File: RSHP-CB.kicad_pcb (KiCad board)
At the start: 2 copper layers, 140 x 120 mm, 23 parts, among them J1 Conn_02x20_Odd_Even, J2 Conn_02x02_Odd_Even, J3 Conn_02x02_Odd_Even, J4 Conn_02x04_Odd_Even

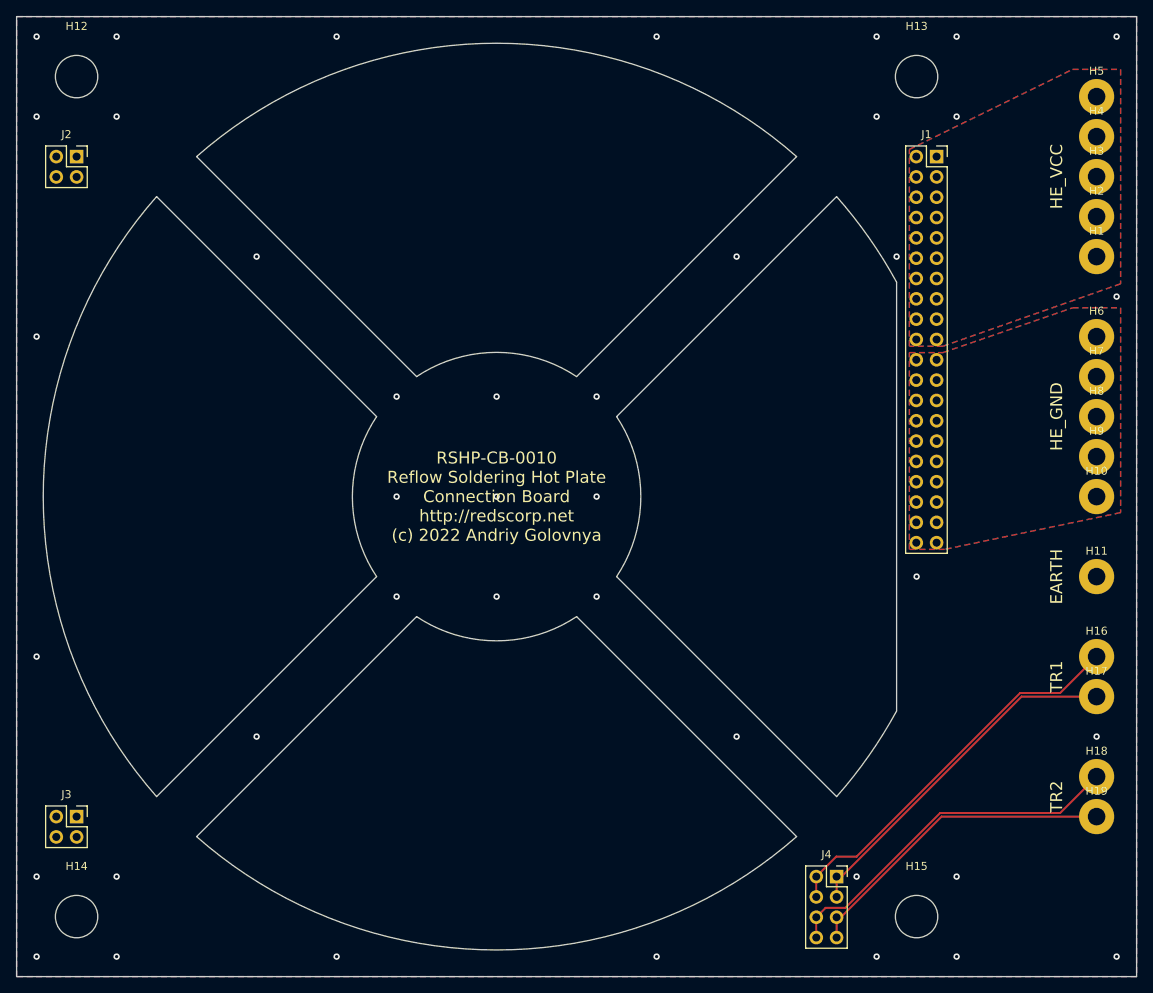
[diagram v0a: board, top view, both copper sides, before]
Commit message: Moved some stuff around on schematics. Added descriptive texts on schematics. Made mount holed current transmissible. Hidden solder and mount holes's designators.
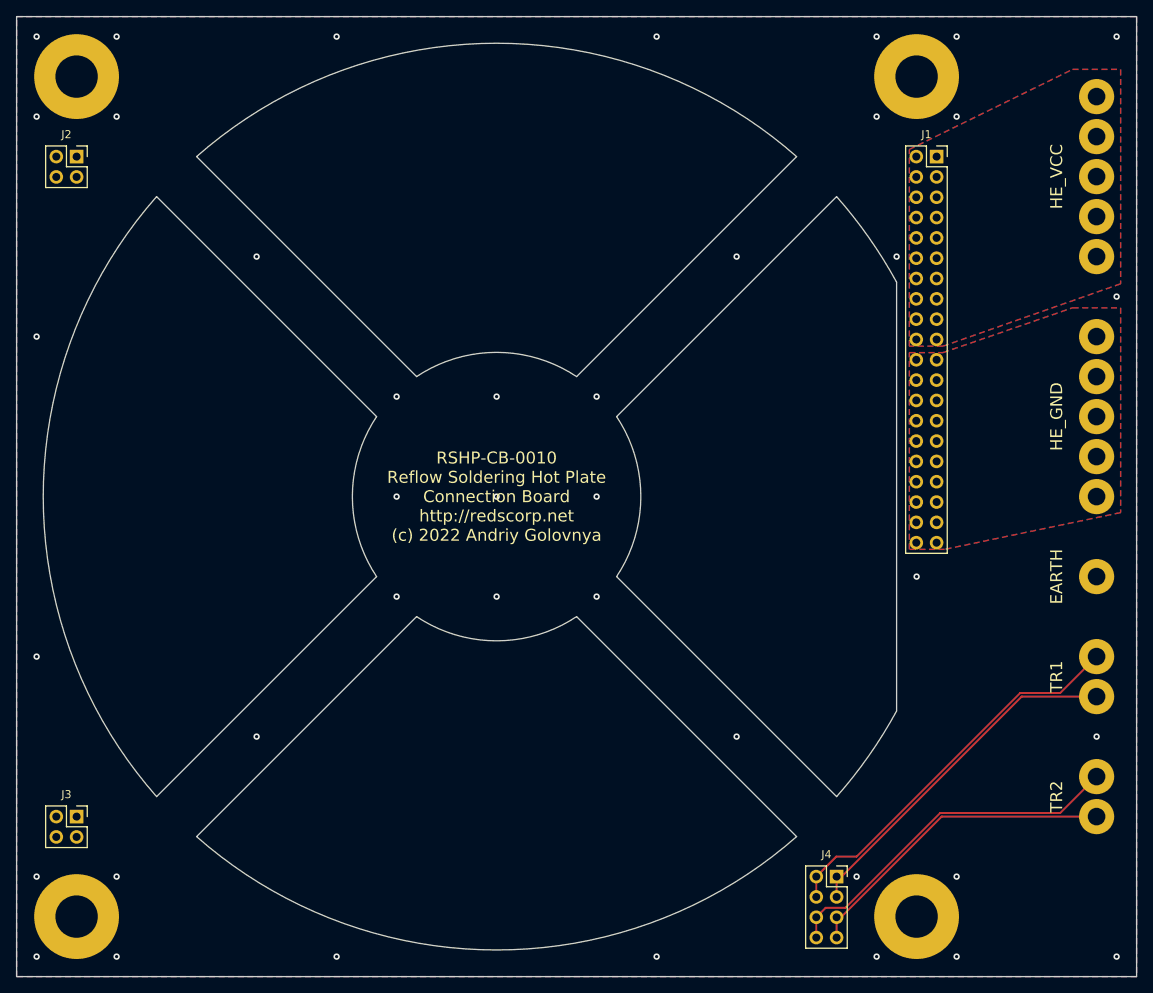
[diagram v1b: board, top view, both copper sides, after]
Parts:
- H12, H13, H14, H15: footprint MountingHole:MountingHole_5.3mm_M5 -> MountingHole:MountingHole_5.3mm_M5_Pad
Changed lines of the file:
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@@
     (property "Sheetname" "")
     (attr exclude_from_pos_files)
-    (fp_text reference "H3" (at 0 -3.2) (layer "F.SilkS")
+    (fp_text reference "H3" (at 0 -3.2) (layer "F.SilkS") hide
       (effects (font (size 1 1) (thickness 0.15)))
     )
@@
     (property "Sheetname" "")
     (attr exclude_from_pos_files)
-    (fp_text reference "H19" (at 0 -3.2) (layer "F.SilkS")
+    (fp_text reference "H19" (at 0 -3.2) (layer "F.SilkS") hide
       (effects (font (size 1 1) (thickness 0.15)))
     )
@@
     (property "Sheetname" "")
     (attr exclude_from_pos_files)
-    (fp_text reference "H18" (at 0 -3.2) (layer "F.SilkS")
+    (fp_text reference "H18" (at 0 -3.2) (layer "F.SilkS") hide
       (effects (font (size 1 1) (thickness 0.15)))
     )
@@
     (property "Sheetname" "")
     (attr exclude_from_pos_files)
-    (fp_text reference "H10" (at 0 -3.2) (layer "F.SilkS")
+    (fp_text reference "H10" (at 0 -3.2) (layer "F.SilkS") hide
       (effects (font (size 1 1) (thickness 0.15)))
     )
@@
     (property "Sheetname" "")
     (attr exclude_from_pos_files)
-    (fp_text reference "H16" (at 0 -3.2) (layer "F.SilkS")
+    (fp_text reference "H16" (at 0 -3.2) (layer "F.SilkS") hide
       (effects (font (size 1 1) (thickness 0.15)))
     )
@@
     (property "Sheetname" "")
     (attr exclude_from_pos_files)
-    (fp_text reference "H8" (at 0 -3.2) (layer "F.SilkS")
+    (fp_text reference "H8" (at 0 -3.2) (layer "F.SilkS") hide
       (effects (font (size 1 1) (thickness 0.15)))
     )
@@
       (net 2 "HE_GND") (pinfunction "1") (pintype "input"))
   )
-  (footprint "MountingHole:MountingHole_5.3mm_M5" (layer "F.Cu")
+  (footprint "MountingHole:MountingHole_5.3mm_M5_Pad" (layer "F.Cu")
     (at 57.5 142.5)
-    (descr "Mounting Hole 5.3mm, no annular, M5")
-    (tags "mounting hole 5.3mm no annular m5")
-    (property "Sheetfile" "RSHP-CB.kicad_sch")
-    (property "Sheetname" "")
-    (attr exclude_from_pos_files)
-    (fp_text reference "H14" (at 0 -6.3) (layer "F.SilkS")
+    (descr "Mounting Hole 5.3mm, M5")
+    (tags "mounting hole 5.3mm m5")
+    (property "Sheetfile" "RSHP-CB.kicad_sch")
+    (property "Sheetname" "")
+    (attr exclude_from_pos_files)
+    (fp_text reference "H14" (at 0 -6.3) (layer "F.SilkS") hide
       (effects (font (size 1 1) (thickness 0.15)))
     )
@@
     (fp_circle (center 0 0) (end 5.3 0) (layer "Cmts.User") (width 0.15) (fill none))
     (fp_circle (center 0 0) (end 5.55 0) (layer "F.CrtYd") (width 0.05) (fill none))
-    (pad "" np_thru_hole circle (at 0 0) (size 5.3 5.3) (drill 5.3) (layers *.Cu *.Mask))
+    (pad "1" thru_hole circle (at 0 0) (size 10.6 10.6) (drill 5.3) (layers *.Cu *.Mask)
+      (net 3 "EARTH") (pinfunction "1") (pintype "input"))
   )
   (footprint "Connector_PinSocket_2.54mm:PinSocket_2x02_P2.54mm_Vertical" (layer "F.Cu")
@@
     (property "Sheetname" "")
     (attr exclude_from_pos_files)
-    (fp_text reference "H6" (at 0 -3.2) (layer "F.SilkS")
+    (fp_text reference "H6" (at 0 -3.2) (layer "F.SilkS") hide
       (effects (font (size 1 1) (thickness 0.15)))
     )
@@
     (property "Sheetname" "")
     (attr exclude_from_pos_files)
-    (fp_text reference "H9" (at 0 -3.2) (layer "F.SilkS")
+    (fp_text reference "H9" (at 0 -3.2) (layer "F.SilkS") hide
       (effects (font (size 1 1) (thickness 0.15)))
     )
@@
       (net 2 "HE_GND") (pinfunction "1") (pintype "input"))
   )
-  (footprint "MountingHole:MountingHole_5.3mm_M5" (layer "F.Cu")
+  (footprint "MountingHole:MountingHole_5.3mm_M5_Pad" (layer "F.Cu")
     (at 57.5 37.5)
-    (descr "Mounting Hole 5.3mm, no annular, M5")
-    (tags "mounting hole 5.3mm no annular m5")
-    (property "Sheetfile" "RSHP-CB.kicad_sch")
-    (property "Sheetname" "")
-    (attr exclude_from_pos_files)
-    (fp_text reference "H12" (at 0 -6.3) (layer "F.SilkS")
+    (descr "Mounting Hole 5.3mm, M5")
+    (tags "mounting hole 5.3mm m5")
+    (property "Sheetfile" "RSHP-CB.kicad_sch")
+    (property "Sheetname" "")
+    (attr exclude_from_pos_files)
+    (fp_text reference "H12" (at 0 -6.3) (layer "F.SilkS") hide
       (effects (font (size 1 1) (thickness 0.15)))
     )
@@
     (fp_circle (center 0 0) (end 5.3 0) (layer "Cmts.User") (width 0.15) (fill none))
     (fp_circle (center 0 0) (end 5.55 0) (layer "F.CrtYd") (width 0.05) (fill none))
-    (pad "" np_thru_hole circle (at 0 0) (size 5.3 5.3) (drill 5.3) (layers *.Cu *.Mask))
-  )
-  (footprint "MountingHole:MountingHole_5.3mm_M5" (layer "F.Cu")
+    (pad "1" thru_hole circle (at 0 0) (size 10.6 10.6) (drill 5.3) (layers *.Cu *.Mask)
+      (net 3 "EARTH") (pinfunction "1") (pintype "input"))
+  )
+  (footprint "MountingHole:MountingHole_5.3mm_M5_Pad" (layer "F.Cu")
     (at 162.5 142.5)
-    (descr "Mounting Hole 5.3mm, no annular, M5")
-    (tags "mounting hole 5.3mm no annular m5")
-    (property "Sheetfile" "RSHP-CB.kicad_sch")
-    (property "Sheetname" "")
-    (attr exclude_from_pos_files)
-    (fp_text reference "H15" (at 0 -6.3) (layer "F.SilkS")
+    (descr "Mounting Hole 5.3mm, M5")
+    (tags "mounting hole 5.3mm m5")
+    (property "Sheetfile" "RSHP-CB.kicad_sch")
+    (property "Sheetname" "")
+    (attr exclude_from_pos_files)
+    (fp_text reference "H15" (at 0 -6.3) (layer "F.SilkS") hide
       (effects (font (size 1 1) (thickness 0.15)))
     )
@@
     (fp_circle (center 0 0) (end 5.3 0) (layer "Cmts.User") (width 0.15) (fill none))
     (fp_circle (center 0 0) (end 5.55 0) (layer "F.CrtYd") (width 0.05) (fill none))
-    (pad "" np_thru_hole circle (at 0 0) (size 5.3 5.3) (drill 5.3) (layers *.Cu *.Mask))
+    (pad "1" thru_hole circle (at 0 0) (size 10.6 10.6) (drill 5.3) (layers *.Cu *.Mask)
+      (net 3 "EARTH") (pinfunction "1") (pintype "input"))
   )
   (footprint "MountingHole:MountingHole_2.2mm_M2_Pad" (layer "F.Cu")
@@
     (property "Sheetname" "")
     (attr exclude_from_pos_files)
-    (fp_text reference "H7" (at 0 -3.2) (layer "F.SilkS")
+    (fp_text reference "H7" (at 0 -3.2) (layer "F.SilkS") hide
       (effects (font (size 1 1) (thickness 0.15)))
     )
@@
       (net 2 "HE_GND") (pinfunction "1") (pintype "input"))
   )
-  (footprint "MountingHole:MountingHole_5.3mm_M5" (layer "F.Cu")
+  (footprint "MountingHole:MountingHole_5.3mm_M5_Pad" (layer "F.Cu")
     (at 162.5 37.5)
-    (descr "Mounting Hole 5.3mm, no annular, M5")
-    (tags "mounting hole 5.3mm no annular m5")
-    (property "Sheetfile" "RSHP-CB.kicad_sch")
-    (property "Sheetname" "")
-    (attr exclude_from_pos_files)
-    (fp_text reference "H13" (at 0 -6.3) (layer "F.SilkS")
+    (descr "Mounting Hole 5.3mm, M5")
+    (tags "mounting hole 5.3mm m5")
+    (property "Sheetfile" "RSHP-CB.kicad_sch")
+    (property "Sheetname" "")
+    (attr exclude_from_pos_files)
+    (fp_text reference "H13" (at 0 -6.3) (layer "F.SilkS") hide
       (effects (font (size 1 1) (thickness 0.15)))
     )
@@
     (fp_circle (center 0 0) (end 5.3 0) (layer "Cmts.User") (width 0.15) (fill none))
     (fp_circle (center 0 0) (end 5.55 0) (layer "F.CrtYd") (width 0.05) (fill none))
-    (pad "" np_thru_hole circle (at 0 0) (size 5.3 5.3) (drill 5.3) (layers *.Cu *.Mask))
+    (pad "1" thru_hole circle (at 0 0) (size 10.6 10.6) (drill 5.3) (layers *.Cu *.Mask)
+      (net 3 "EARTH") (pinfunction "1") (pintype "input"))
   )
   (footprint "MountingHole:MountingHole_2.2mm_M2_Pad" (layer "F.Cu")
@@
     (property "Sheetname" "")
     (attr exclude_from_pos_files)
-    (fp_text reference "H11" (at 0 -3.2) (layer "F.SilkS")
+    (fp_text reference "H11" (at 0 -3.2) (layer "F.SilkS") hide
       (effects (font (size 1 1) (thickness 0.15)))
     )
@@
     (property "Sheetname" "")
     (attr exclude_from_pos_files)
-    (fp_text reference "H2" (at 0 -3.2) (layer "F.SilkS")
+    (fp_text reference "H2" (at 0 -3.2) (layer "F.SilkS") hide
       (effects (font (size 1 1) (thickness 0.15)))
     )
@@
     (property "Sheetname" "")
     (attr exclude_from_pos_files)
-    (fp_text reference "H17" (at 0 -3.2) (layer "F.SilkS")
+    (fp_text reference "H17" (at 0 -3.2) (layer "F.SilkS") hide
       (effects (font (size 1 1) (thickness 0.15)))
     )
@@
     (property "Sheetname" "")
     (attr exclude_from_pos_files)
-    (fp_text reference "H1" (at 0 -3.2) (layer "F.SilkS")
+    (fp_text reference "H1" (at 0 -3.2) (layer "F.SilkS") hide
       (effects (font (size 1 1) (thickness 0.15)))
     )
@@
     (property "Sheetname" "")
     (attr exclude_from_pos_files)
-    (fp_text reference "H5" (at 0 -3.2) (layer "F.SilkS")
+    (fp_text reference "H5" (at 0 -3.2) (layer "F.SilkS") hide
       (effects (font (size 1 1) (thickness 0.15)))
     )
@@
     (property "Sheetname" "")
     (attr exclude_from_pos_files)
-    (fp_text reference "H4" (at 0 -3.2) (layer "F.SilkS")
-      (effects (font (size 1 1) (thickness 0.15)))
-    )
+    (fp_text reference "H4" (at 0 -3.2) (layer "F.SilkS") hide
+      (effects (font (size 1 1) (thickness 0.15)))
+    )
